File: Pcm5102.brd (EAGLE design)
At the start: 39.6 x 22.6 mm, 24 parts

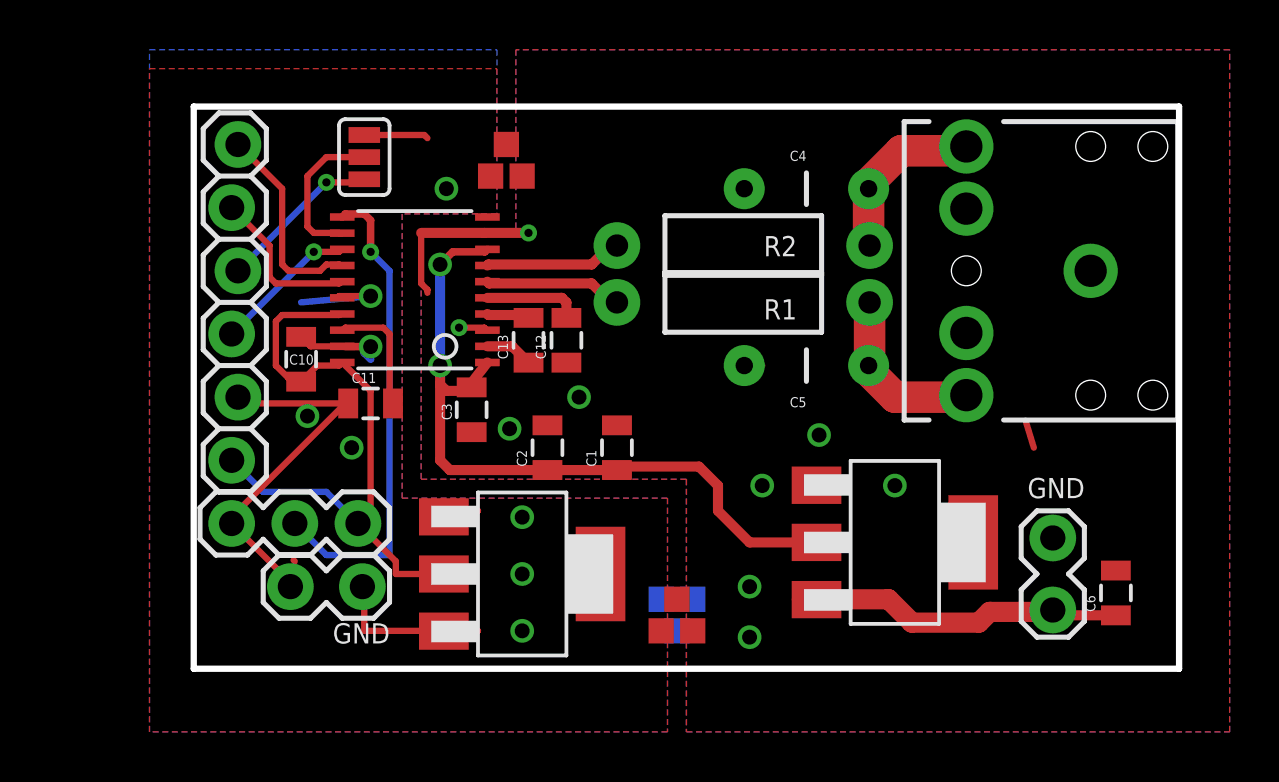
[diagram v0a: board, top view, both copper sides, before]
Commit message: V1.2
Change LDO from LM1117 to LP5907 (Ultra Low noise)
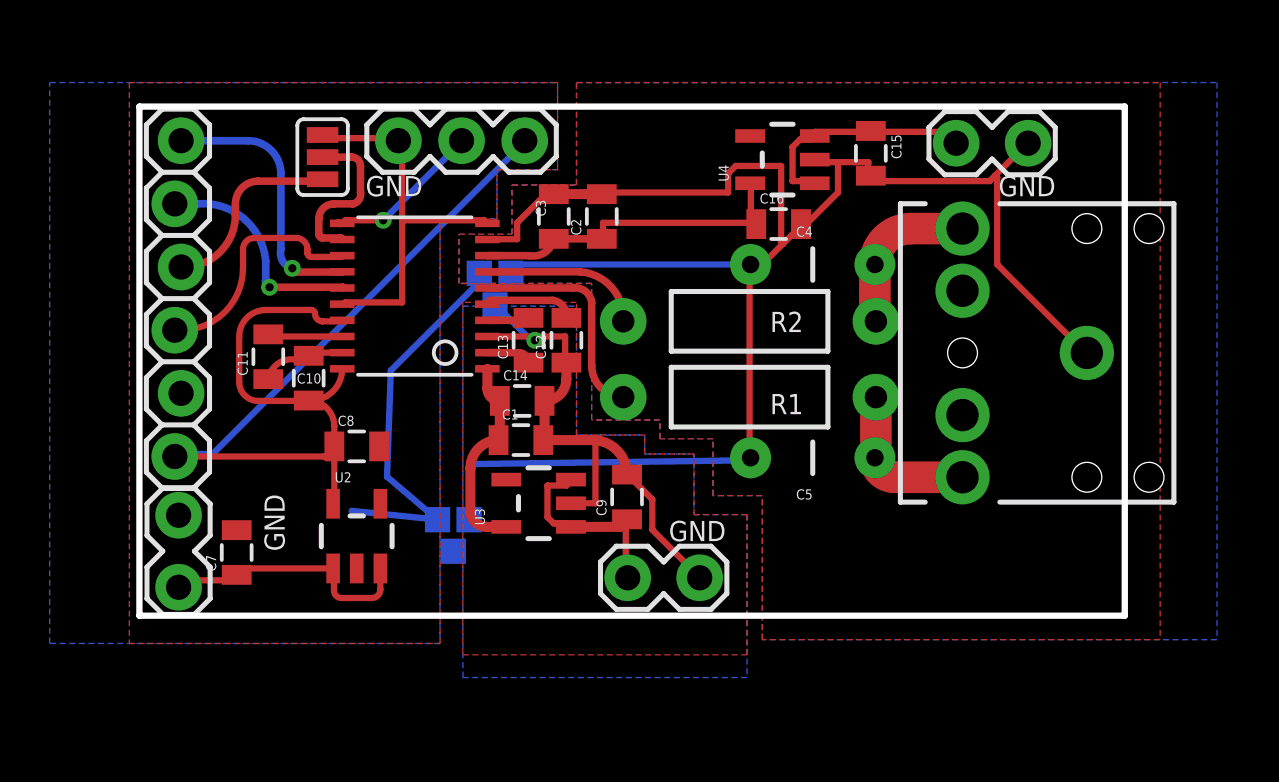
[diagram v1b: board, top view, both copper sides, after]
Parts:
- removed C6: (no value), SparkFun-Capacitors:0805
- removed U$4: GND_CONNECT, SparkFun-Passives:GND_CONNECT
- removed VREG1, VREG3: (no value), dp_devices:SOT-223
- added C14, C15, C16, C7, C8, C9: (no value), SparkFun-Capacitors:0805
- added JP4: M02LOCK, SparkFun-Connectors:1X02_LOCK
- added U2: DVCC, SparkFun-PowerIC:SOT23-5
- added U3: CPVDD, SparkFun-PowerIC:SOT23-5
- added U4: AVDD, SparkFun-PowerIC:SOT23-5
- moved JP1 16.8 mm to (22.7, 33.9)
- moved JP6 14.4 mm to (34.6, 16.4), turned to 180 degrees
- moved U$2 14.3 mm to (26.0, 27.6), flipped to the bottom, turned to 270 degrees
- moved C2 9.55 mm to (30.9, 30.9)
- moved U$3 9.54 mm to (24.3, 17.7)
- moved C3 8.44 mm to (29.0, 30.9), turned to 90 degrees
- moved JP7 5.39 mm to (13.9, 18.7), turned to 270 degrees
- moved C11 4.52 mm to (17.5, 25.2), turned to 90 degrees
- moved C1 3.87 mm to (27.6, 21.9), turned to 0 degrees
- moved R1 3.82 mm to (36.8, 23.6)
- moved C5 3.72 mm to (39.4, 21.2)
- moved U1 3.31 mm to (50.4, 25.4)
- moved C4 3.06 mm to (39.4, 29.0)
- moved R2 3.06 mm to (36.8, 26.7)
- moved JP2 2.29 mm to (13.7, 21.2)
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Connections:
- removed net AVCC: C1.1, C2.1, C3.1, U$1.1, U$1.8, VREG1.2
- removed net AVCCIN: C6.1, JP6.2, VREG1.3
- removed net DVCCIN: JP7.2, VREG3.3
- removed net DVDD: U$1.17
- new net AVDD: C16.1, C2.1, C3.1, U$1.8, U4.5
- new net CPGND: C1.2, C12.1, C14.2, C9.2, JP6.1, U$1.3, U$2.3, U3.2
- new net CPVDD: C1.1, C14.1, U$1.1, U3.5
- new net N$10: C15.1, JP4.2, U4.1, U4.3
- new net N$15: C9.1, JP6.2, U3.1, U3.3
- new net N$16: C7.1, JP7.2, U2.1, U2.3
- net AGND: now also C15.2, C16.2, JP4.1, U4.2; no longer C1.2, C12.1, C6.2, JP6.1, U$1.3, U$4.2, VREG1.1
- net DGND: now also C7.2, C8.2, U2.2; no longer U$4.1, VREG3.1
- net DVCC: now also C8.1, U$1.17, U2.5; no longer VREG3.2
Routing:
- net AGND: track 9.74 -> 73.4 mm, vias 9 -> 0
- net AVCC: track 30.1 -> 0.00 mm, vias 2 -> 0
- net CPGND: track 0.00 -> 23.1 mm, vias 0 -> 1
- net DVCC: track 20.1 -> 42.4 mm
- net AVCCIN: track 14.1 -> 0.00 mm
- net AVDD: track 0.00 -> 13.4 mm
- net N$3: track 19.4 -> 6.38 mm
- net N$16: track 0.00 -> 10.6 mm
- net N$10: track 0.00 -> 9.69 mm
- net CPVDD: track 0.00 -> 8.12 mm
- net DGND: track 27.8 -> 35.9 mm, vias 8 -> 0
- net N$15: track 0.00 -> 7.98 mm
- net DVCCIN: track 7.80 -> 0.00 mm
- net DVDD: track 5.79 -> 0.00 mm
- net BCK: track 5.85 -> 9.14 mm, vias 1 -> 0
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- added copper zone on layer 1, net CPGND
- added copper zone on layer 16, net CPGND
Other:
- board size 39.6 x 22.6 mm -> 39.6 x 20.5 mm
